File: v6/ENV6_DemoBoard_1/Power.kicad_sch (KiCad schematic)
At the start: 69 parts, among them J201 Conn_01x02_Pin, J202 Conn_01x02_Pin, J203 Conn_01x02_Pin, J204 Conn_01x02_Pin, Q201 2N7002E, Q202 2N7002E, Q203 2N7002E, Q204 2N7002E, U201 BQ25188, U202 MAX20029ATIA_V+

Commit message: ENV6 (test): Changes after first review
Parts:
- removed C203, C204: 100n, Capacitor_SMD:C_0402_1005Metric, symbol passive:C0402
- removed D201, D202: LED, LED_SMD:LED_0402_1005Metric, symbol Device:LED
- removed R204, R205: 1kR, Resistor_SMD:R_0402_1005Metric, symbol Device:R
- removed S201: TL3365AF180QG, ui_stuff:TL3365AF180QG, symbol TL3365AF180QG:TL3365AF180QG
- removed TP1, TP8: TestPoint_Probe, TestPoint:TestPoint_Pad_1.0x1.0mm, symbol Connector:TestPoint_Probe
- added R3: 4.7kR, Resistor_SMD:R_0402_1005Metric, symbol Device:R
- added R4: 47kR, Resistor_SMD:R_0402_1005Metric, symbol Device:R
- added S6: BTN, connectors:TACTILE-SWITCH, symbol connectors:Tactile Button
- added TP1: TestPoint, custom_library:TestPoint_Pad_D1.0mm, symbol passive:TestPoint
- C202: value 100n -> 10µ
- C205: value 1uF -> 1µ
- C206, C208: value 100nF -> 100n
- C207: value 10uF -> 10µ
- C209: value 1uF -> 1u
- R201, R202: value 5.1kR -> 5k1
- R203: value 470R -> 5k1
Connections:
- net GND: now also R203.2
- net V_SYS: now also TP1.1
- net at J_BATT1.2, U201.D1 (TS/MR): now also S6.1, S6.2 (1)
- new net: S6.3 (2), S6.4 (2)
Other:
- note added: "1.0 - 1.2 V / FPGA core"
- note added: "1.8 V - 1.2 V / FPGA core"
- note added: "3.3 V - 1.8 V / FPGA bank"
- note added: "3.3V / MCU"
- note added: "Add resistor to Line 4 (but not assembled) application-specific"
- note added: "Also just move to the MCU (with pull-up) and remove transistors and LEDs"
- note added: "Connecting all GPIOs to MCU"
- note added: "Find a PMU with programmable output voltage using I2C"
- note added: "I would add these to the MCU and remove the headers Permanent enable of the line to the mcu - PWR for MCU should be enabled permanently"
- note added: "Question - Move PSU to FPGA board? - Add additional simple DCDC converter for powering MCU?"
- note removed: "1.0V"
- note removed: "1.1V"
- note removed: "1.8V"
- note removed: "3.3V"
- moved on the sheet: C201, C202

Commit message: new PSU and updates
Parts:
- removed C210, C211, C212, C213: 2.2uF, Capacitor_SMD:C_0402_1005Metric, symbol passive:C0402
- removed C214: 1uF, Capacitor_SMD:C_0402_1005Metric, symbol passive:C0402
- removed C215: 10uF, Capacitor_SMD:C_0402_1005Metric, symbol passive:C0402
- removed C216: 15pF, Capacitor_SMD:C_0402_1005Metric, symbol passive:C0402
- removed C217: 20uF, Capacitor_SMD:C_0402_1005Metric, symbol passive:C0402
- removed C218: 18pF, Capacitor_SMD:C_0402_1005Metric, symbol passive:C0402
- removed C219, C221: 27uF, Capacitor_SMD:C_0402_1005Metric, symbol passive:C0402
- removed C220: 150pF, Capacitor_SMD:C_0402_1005Metric, symbol passive:C0402
- removed D203, D204, D205, D206: LED, LED_SMD:LED_0402_1005Metric, symbol Device:LED
- removed J201, J202, J203, J204: Conn_01x02_Pin, Connector_PinSocket_2.54mm:PinSocket_1x02_P2.54mm_Vertical, symbol Connector:Conn_01x02_Pin
- removed L201, L202, L203: 1.5uH, Inductor_SMD:L_1008_2520Metric, symbol Device:L
- removed Q201, Q202, Q203, Q204: 2N7002E, Package_TO_SOT_SMD:SOT-23, symbol Transistor_FET:2N7002E
- removed R206, R207, R208, R209, R210, R211, R212, R213, R217: 10kR, Resistor_SMD:R_0402_1005Metric, symbol Device:R
- removed R214: 30kR, Resistor_SMD:R_0402_1005Metric, symbol Device:R
- removed R215: 13kR, Resistor_SMD:R_0402_1005Metric, symbol Device:R
- removed R216: 8.2kR, Resistor_SMD:R_0402_1005Metric, symbol Device:R
- removed R218, R3: 4.7kR, Resistor_SMD:R_0402_1005Metric, symbol Device:R
- removed R219, R4: 47kR, Resistor_SMD:R_0402_1005Metric, symbol Device:R
- removed R222, R223, R224, R225: 1kR, Resistor_SMD:R_0402_1005Metric, symbol Device:R
- removed S6: BTN, connectors:TACTILE-SWITCH, symbol connectors:Tactile Button
- removed U202: MAX20029ATIA_V+, custom_library:QFN50P500X500X80-29N, symbol MAX20029ATIA_V+:MAX20029ATIA_V+
- added C1, C10, C11, C13, C2, C3, C4: 22µ, Capacitor_SMD:C_0402_1005Metric, symbol passive:C0402
- added C12: 47µ, Capacitor_SMD:C_0402_1005Metric, symbol passive:C0402
- added C5, C6, C7, C8, C9: 10µ, Capacitor_SMD:C_0402_1005Metric, symbol passive:C0402
- added IC1: LP8758A2EAYFFR, custom_library:BGA35C40P5X7_213X288X62, symbol LP8758A2EAYFFR:LP8758A2EAYFFR
- added L1, L2, L3: 0.47uH, Inductor_SMD:L_1008_2520Metric, symbol Device:L
- added R204: 10k, Resistor_SMD:R_0402_1005Metric, symbol passive:R0402
- added R3: 511k, Resistor_SMD:R_0402_1005Metric, symbol passive:R0402
- added R303: 0, Resistor_SMD:R_0402_1005Metric, symbol passive:R0402
- added R4: 91k, Resistor_SMD:R_0402_1005Metric, symbol passive:R0402
- added U1: TPSM8310x, custom_library:MICROSIP8_SIU_TEX, symbol power_devices:TPSM83100
- C209: value 1u -> 1µ
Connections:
- net GND: now also J_BATT1.2, C1.1, C10.1, C11.1, C12.1, C13.1, C2.1, C3.1, C4.1, C5.1, C6.1, C7.1, C8.1, C9.1, IC1.A3 (PGND_B01_1), IC1.B3 (PGND_B01_2), IC1.C1 (SGND_&_GNDs), IC1.C3 (PGND_B01_3), IC1.D1 (AGND), IC1.E3 (PGND_B23_1), IC1.F3 (PGND_B23_2), IC1.G3 (PGND_B23_3), R204.2, R4.2, U1.2 (GND), U1.3 (GND), U1.6 (GND), U1.7 (MODE)
- net GP0/I2C0_SDA: now also IC1.D5 (SDA)
- net GP1/I2C0_SCL: now also IC1.E5 (SCL)
- net PSU_OUT1: now also C1.2, IC1.C4 (FB_B0), L1.2
- net PSU_OUT2: now also C2.2, IC1.C2 (FB_B1), L2.2
- net PSU_OUT3: now also C3.2, IC1.E4 (FB_B2), L3.2
- net PSU_OUT4: now also C4.2, IC1.E2 (FB_B3)
- net V_SYS: now also C10.2, C11.2, C13.2, C5.2, C6.2, C7.2, C8.2, C9.2, IC1.A1 (VIN_B1_1), IC1.A5 (VIN_B0_1), IC1.B1 (VIN_B1_2), IC1.B5 (VIN_B0_2), IC1.E1 (VANA), IC1.F1 (VIN_B3_1), IC1.F5 (VIN_B2_1), IC1.G1 (VIN_B3_2), IC1.G5 (VIN_B2_2), U1.1 (VIN), U1.8 (EN)
- net at U201.D1 (TS/MR): now also R204.1, R303.1; no longer J_BATT1.2
- net at L204.1: now also IC1.F2 (SW_B3_1), IC1.G2 (SW_B3_2)
- new net: IC1.A2 (SW_B1_1), IC1.B2 (SW_B1_2), L2.1
- new net: IC1.A4 (SW_B0_1), IC1.B4 (SW_B0_2), L1.1
- new net: IC1.F4 (SW_B2_1), IC1.G4 (SW_B2_2), L3.1
- new net: R3.2, R4.1, U1.5 (FB)
- new net 3V3_MCU: C12.2, R3.1, U1.4 (VOUT)
- new net BQ_TS/MR: R303.2
- new net LP_EN1: IC1.C5 (EN1)
- new net LP_EN2: IC1.D3 (EN2)
- new net LP_NRST: IC1.D4 (NRST)
- new net LP_nINT: IC1.D2 (NINT)
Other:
- note added: "3.3V / FPGA"
- note removed: "2.2uF placed close to each PV. 1uF close to VA"
- note removed: "3.3V / MCU"
- note removed: "Add resistor to Line 4 (but not assembled) application-specific"
- note removed: "Find a PMU with programmable output voltage using I2C"
- note removed: "SYNC set to GND -> default switching Freq"
- moved on the sheet: C209, L204

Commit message: Changes after second rev of ENV6 test
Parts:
- removed C11, C2, C3, C4: 22µ, Capacitor_SMD:C_0402_1005Metric, symbol passive:C0402
- removed IC1: LP8758A2EAYFFR, custom_library:BGA35C40P5X7_213X288X62, symbol LP8758A2EAYFFR:LP8758A2EAYFFR
- removed R303: 0, Resistor_SMD:R_0402_1005Metric, symbol passive:R0402
- removed U201: BQ25188, Package_BGA:Texas_DSBGA-8_0.9x1.9mm_Layout2x4_P0.5mm, symbol common_library:BQ25188
- added C28, C32, C34, C35, C37, C38, C41, C42: 10u, Capacitor_SMD:C_0402_1005Metric, symbol passive:C0402
- added IC1: LP8758-A2EA-YFFR, custom_library:BGA35C40P5X7_213X288X62, symbol power_devices:LP8758A2EAYFFR
- added TP3: TestPoint, custom_library:TestPoint_Pad_D1.0mm, symbol passive:TestPoint
- added U4: BQ25188, Package_BGA:Texas_DSBGA-8_0.9x1.9mm_Layout2x4_P0.5mm, symbol power_devices:BQ25188
- C19: renamed from C205; value 1µ -> 10u
- C22: renamed from C202; value 10µ -> 10u
- C23: renamed from C207; value 10µ -> 10u
- C25: renamed from C209; value 1µ -> 10u
- C29: renamed from C10; value 22µ -> 10u
- C30: renamed from C5; value 10µ -> 10u
- C31: renamed from C1; value 22µ -> 10u
- C33: renamed from C6; value 10µ -> 10u
- C36: renamed from C7; value 10µ -> 10u
- C39: renamed from C12; value 47µ -> 10u
- C40: renamed from C8; value 10µ -> 10u
- C43: renamed from C13; value 22µ -> 10u
- C44: renamed from C9; value 10µ -> 10u
- R12: renamed from R204; now fitted; now in the parts list
- renumbered C206 to C20, C201 to C21, C208 to C24, L1 to L2, L2 to L3, L3 to L4, L204 to L5, R201 to R10, R202 to R11, R203 to R13, R3 to R19, R4 to R20, TP1 to TP2, U1 to U6
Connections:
- net GND: now also C28.1, C32.1, C34.1, C35.1, C37.1, C38.1, C41.1, C42.1, IC1.A3 (PGND_B01_1), IC1.B3 (PGND_B01_2), IC1.C1 (SGND_&_GNDs), IC1.C3 (PGND_B01_3), IC1.D1 (AGND), IC1.E3 (PGND_B23_1), IC1.F3 (PGND_B23_2), IC1.G3 (PGND_B23_3), U4.D2 (GND)
- net GP0/I2C0_SDA: now also IC1.D5 (SDA), U4.C1 (SDA)
- net GP1/I2C0_SCL: now also IC1.E5 (SCL), U4.B1 (SCL)
- net PSU_OUT1: now also C32.2, IC1.C4 (FB_B0)
- net PSU_OUT2: now also C34.2, C35.2, IC1.C2 (FB_B1)
- net PSU_OUT3: now also C37.2, C38.2, IC1.E4 (FB_B2)
- net PSU_OUT4: now also C41.2, C42.2, IC1.E2 (FB_B3)
- net USB_VCC: now also U4.A2 (IN)
- net at C25.1, J_BATT1.1: now also U4.C2 (BAT)
- net at R12.1: now also U4.D1 (TS/MR)
- net at L3.1: now also IC1.A2 (SW_B1_1), IC1.B2 (SW_B1_2)
- net at L2.1: now also IC1.A4 (SW_B0_1), IC1.B4 (SW_B0_2)
- net at L5.1: now also IC1.F2 (SW_B3_1), IC1.G2 (SW_B3_2)
- net at L4.1: now also IC1.F4 (SW_B2_1), IC1.G4 (SW_B2_2)
- net 3V3_MCU renamed VDIG_OUT
- net VDIG_OUT: now also TP3.1
- net V_SYS renamed VFPGA_IN
- net VFPGA_IN: now also C28.2, IC1.A1 (VIN_B1_1), IC1.A5 (VIN_B0_1), IC1.B1 (VIN_B1_2), IC1.B5 (VIN_B0_2), IC1.E1 (VANA), IC1.F1 (VIN_B3_1), IC1.F5 (VIN_B2_1), IC1.G1 (VIN_B3_2), IC1.G5 (VIN_B2_2); no longer C23.1, C24.1, C43.2, TP2.1, U6.1 (VIN), U6.8 (EN)
- new net VDIG_IN: C43.2, U6.1 (VIN), U6.8 (EN)
- new net VSYS_IN: C23.1, C24.1, TP2.1, U4.B2 (SYS)
- no-connect marks 2 -> 7
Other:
- note added: "Can we use all pins also using I2C? If yes, remove all And what happens with them if we do not use it?"
- note added: "Can we use also the same with three channels?"
- note added: "Digital Power Supply"
- note added: "I2C Addr: 0x60"
- note added: "I2C Addr: 0x6A"
- note added: "Power Supply Unit"
- note added: "default reading"
- note removed: "Also just move to the MCU (with pull-up) and remove transistors and LEDs"
- note removed: "Connecting all GPIOs to MCU"
- note removed: "I would add these to the MCU and remove the headers Permanent enable of the line to the mcu - PWR for MCU should be enabled permanently"
- note removed: "PSU"
- note removed: "Question - Move PSU to FPGA board? - Add additional simple DCDC converter for powering MCU?"
- moved on the sheet: C31, C39, C43, R10, R11, R13, R19, R20, TP2

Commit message: added comments
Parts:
- added R37: 10k, Resistor_SMD:R_0402_1005Metric, symbol passive:R0402
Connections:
- net VFPGA_IN: now also R37.1
- net at IC1.D4 (NRST): now also R37.2
- no-connect marks 7 -> 6
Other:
- note added: "Can we use all pins also using I2C? If yes, remove all And what happens with them if we do not use it? EN_BUCKn in Registers can Enable BUCKn without EN1/2 Reset can be software commanded from Reg 0x16 nRST Low = shutdown. nRST High = startup. Pull up nRST."
- note added: "Can we use also the same with three channels? only 4 outputs availabe, to make it 3 needs to combine 2 outputs into 1"
- note removed: "Can we use all pins also using I2C? If yes, remove all And what happens with them if we do not use it?"
- note removed: "Can we use also the same with three channels?"
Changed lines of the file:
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@@
 		)
 	)
-	(text "Can we use all pins also using I2C?\nIf yes, remove all\nAnd what happens with them if we do not use it?"
+	(text "Can we use all pins also using I2C?\nIf yes, remove all\nAnd what happens with them if we do not use it?\n\nEN_BUCKn in Registers can Enable BUCKn without EN1/2\nReset can be software commanded from Reg 0x16\n\nnRST Low = shutdown. nRST High = startup.\nPull up nRST.\n"
 		(exclude_from_sim no)
-		(at 65.786 182.88 0)
+		(at 62.23 196.342 0)
 		(effects
 			(font
@@
 		)
 	)
-	(text "Can we use also the same with three channels?"
+	(text "Can we use also the same with three channels?\nonly 4 outputs availabe, \nto make it 3 needs to combine 2 outputs into 1"
 		(exclude_from_sim no)
-		(at 139.954 161.29 0)
+		(at 141.732 164.592 0)
 		(effects
 			(font
@@
 	)
 	(junction
+		(at 55.88 156.21)
+		(diameter 0)
+		(color 0 0 0 0)
+	)
+	(junction
 		(at 138.43 140.97)
 		(diameter 0)
@@
 	)
 	(no_connect
-		(at 68.58 181.61)
-	)
-	(no_connect
 		(at 58.42 49.53)
 	)
@@
 	(wire
 		(pts
+			(xy 34.29 165.1) (xy 34.29 156.21)
+		)
+		(stroke
+			(width 0)
+			(type default)
+		)
+	)
+	(wire
+		(pts
 			(xy 213.36 123.19) (xy 213.36 130.81)
 		)
@@
 	(wire
 		(pts
+			(xy 34.29 181.61) (xy 34.29 172.72)
+		)
+		(stroke
+			(width 0)
+			(type default)
+		)
+	)
+	(wire
+		(pts
 			(xy 240.03 138.43) (xy 240.03 139.7)
 		)
@@
 	(wire
 		(pts
+			(xy 68.58 181.61) (xy 34.29 181.61)
+		)
+		(stroke
+			(width 0)
+			(type default)
+		)
+	)
+	(wire
+		(pts
 			(xy 85.09 59.69) (xy 88.9 59.69)
 		)
@@
 	(wire
 		(pts
+			(xy 34.29 156.21) (xy 55.88 156.21)
+		)
+		(stroke
+			(width 0)
+			(type default)
+		)
+	)
+	(wire
+		(pts
 			(xy 222.25 63.5) (xy 219.71 63.5)
 		)
@@
 					(unit 1)
 				)
+			)
+		)
+	)
+	(symbol
+		(lib_id "passive:R0402")
+		(at 34.29 168.91 0)
+		(unit 1)
+		(exclude_from_sim no)
+		(in_bom yes)
+		(on_board yes)
+		(dnp no)
+		(fields_autoplaced yes)
+		(property "Reference" "R37"
+			(at 36.83 167.6399 0)
+			(effects
+				(font
+					(size 1.27 1.27)
+				)
+				(justify left)
+			)
+		)
+		(property "Value" "10k"
+			(at 36.83 170.1799 0)
+			(effects
+				(font
+					(size 1.27 1.27)
+				)
+				(justify left)
+			)
+		)
+		(property "Footprint" "Resistor_SMD:R_0402_1005Metric"
+			(at 32.512 168.91 90)
+			(effects
+				(font
+					(size 1.27 1.27)
+				)
+				(hide yes)
+			)
+		)
+		(property "Datasheet" "~"
+			(at 34.29 168.91 0)
+			(effects
+				(font
+					(size 1.27 1.27)
+				)
+				(hide yes)
+			)
+		)
+		(property "Description" "Resistor"
+			(at 34.29 168.91 0)
+			(effects
+				(font
+					(size 1.27 1.27)
+				)
+				(hide yes)
+			)
+		)
+		(pin "2"
+		)
+		(pin "1"
+		)
+		(instances
+			(project "ENV6_DemoBoard_1"
+				(path "/c353698e-fca1-4ed3-95bc-4f5142868012/902366bc-6ca4-48af-8389-df3fa638596e"
+					(reference "R37")
+					(unit 1)
+				)

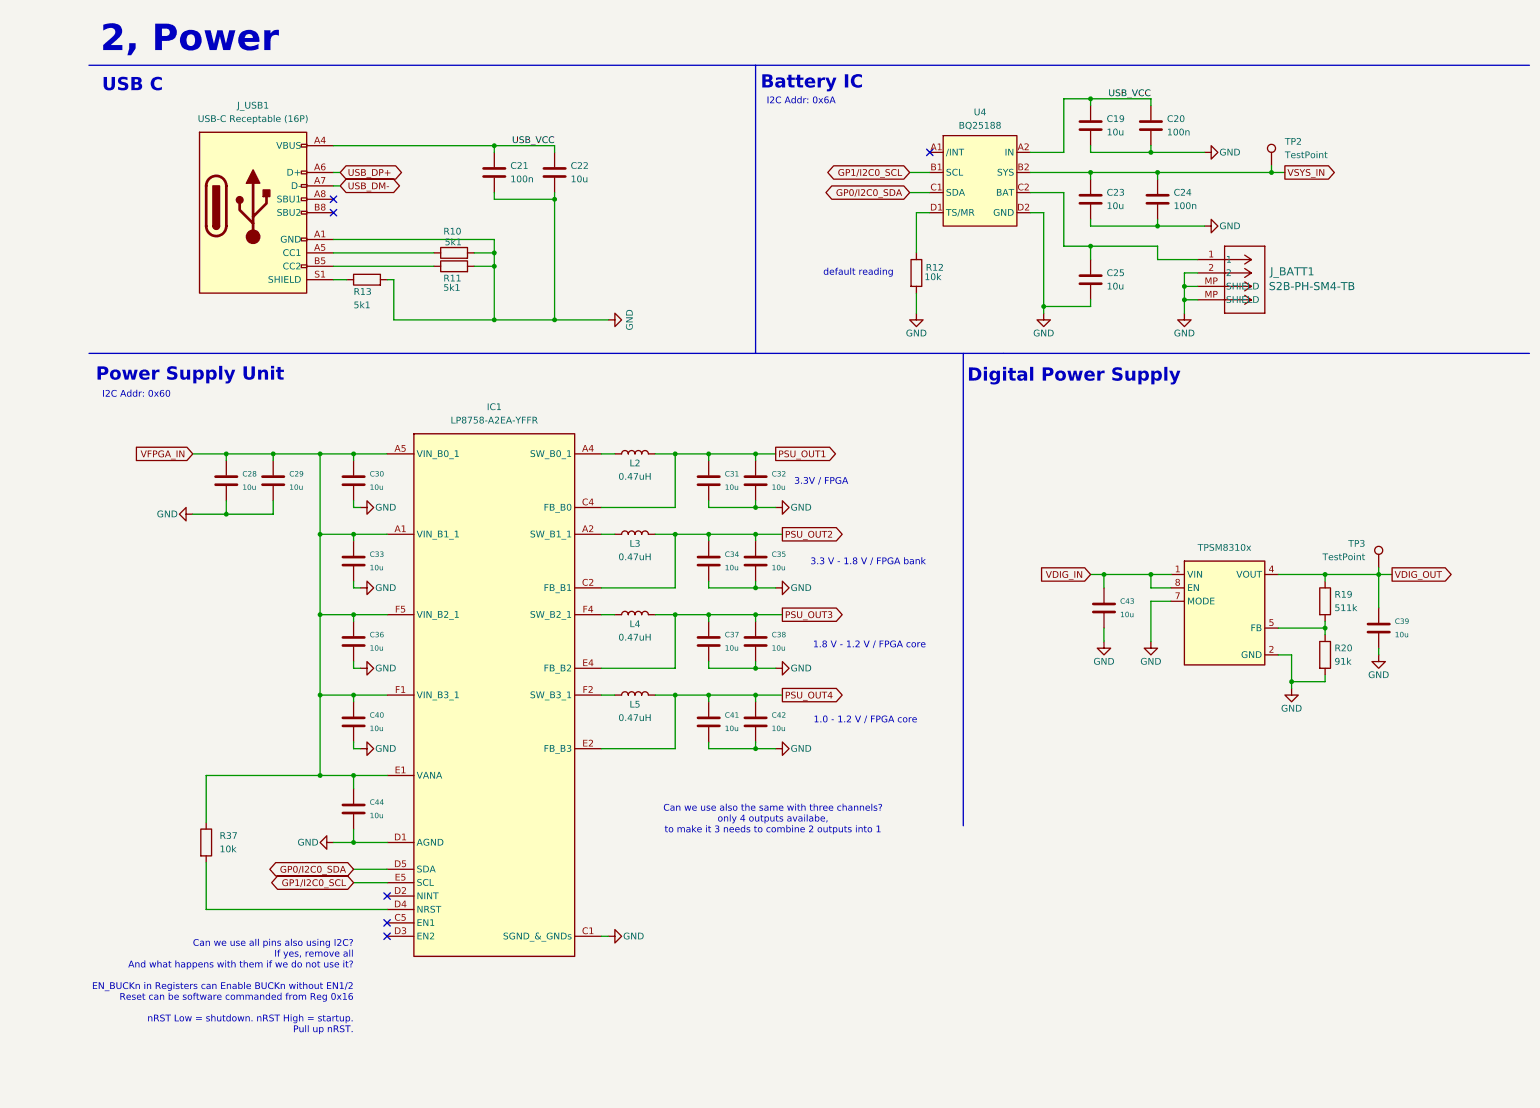
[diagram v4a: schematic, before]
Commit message: update Demoboard and add GateMateA11 board
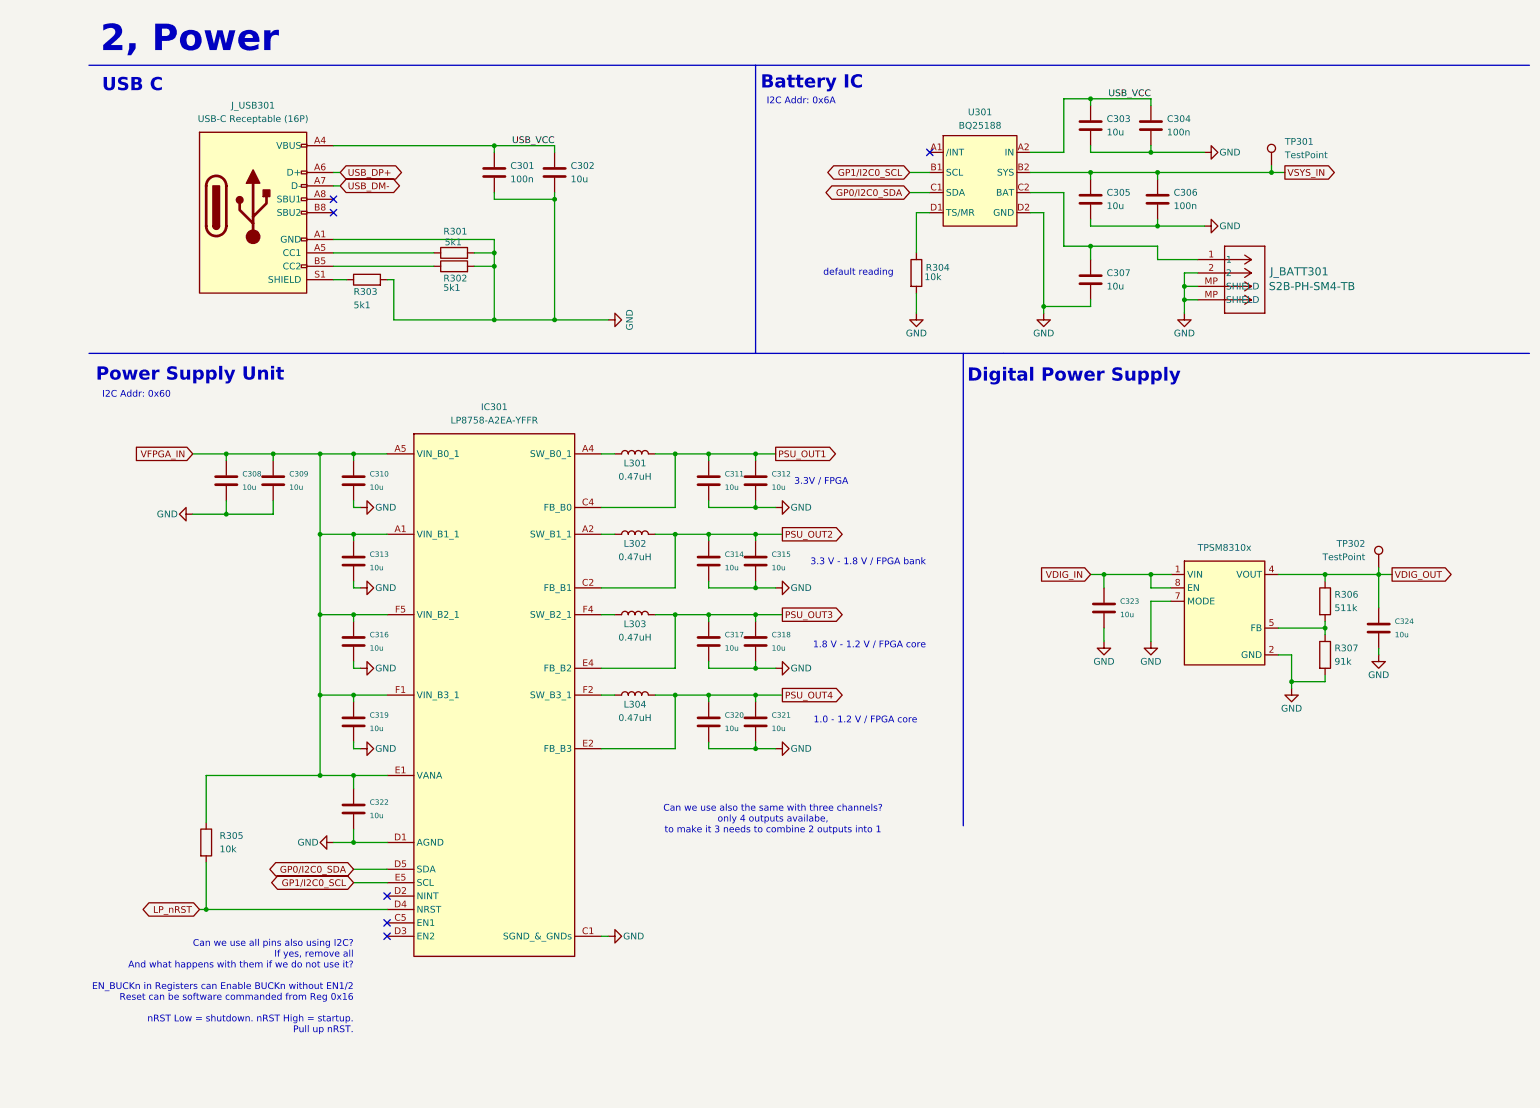
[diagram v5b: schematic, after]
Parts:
- renumbered C21 to C301, C22 to C302, C19 to C303, C20 to C304, C23 to C305, C24 to C306, C25 to C307, C28 to C308, C29 to C309, C30 to C310, C31 to C311, C32 to C312, C33 to C313, C34 to C314, C35 to C315, C36 to C316, C37 to C317, C38 to C318, C40 to C319, C41 to C320, C42 to C321, C44 to C322, C43 to C323, C39 to C324, IC1 to IC301, J_BATT1 to J_BATT301, J_USB1 to J_USB301, L2 to L301, L3 to L302, L4 to L303, L5 to L304, R10 to R301, R11 to R302, R13 to R303, R12 to R304, R37 to R305, R19 to R306, R20 to R307, TP2 to TP301, TP3 to TP302, U4 to U301, U6 to U302
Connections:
- net LP_nRST: now reaches IC301.D4 (NRST), R305.2
